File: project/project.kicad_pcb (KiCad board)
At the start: 4 copper layers, 64.5 x 86 mm, 186 parts, among them J101 BUS, J102 rs485, J103 qwiic, J104 FFC, J105 Bot, J106 FFC, J107 Top, J108 Mid, J109 Mid, J110 USB_C_Receptacle_USB2.0, J111 BUS, J201 5V, J202 24V, J203 3V3, J401 RJ45_Shielded, SW101 15mm, SW102 15mm, U101 TMP102, U102 24C02S, U103 USBLC6-2SC6, U104 TMP102, U105 INA226, U201 DP9700AT-24, U202 ME3121AM6G, U203 JTD6206-3.3V, U301 esp32-C3FH4X, U401 W5500, U501 XL1050, U601 MAX13487E, Y301 40MHz, Y401 25MHz

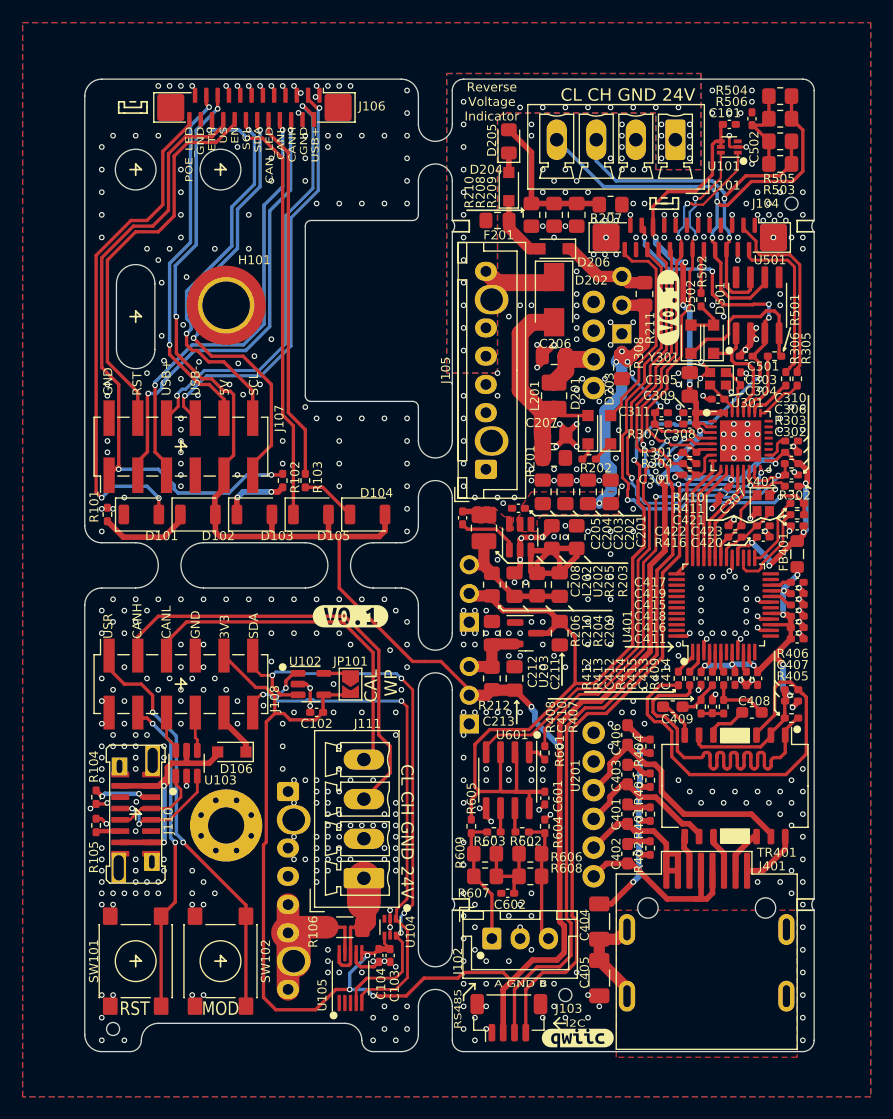
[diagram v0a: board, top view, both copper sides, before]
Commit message: fix PSU FB and tmp102 pinout
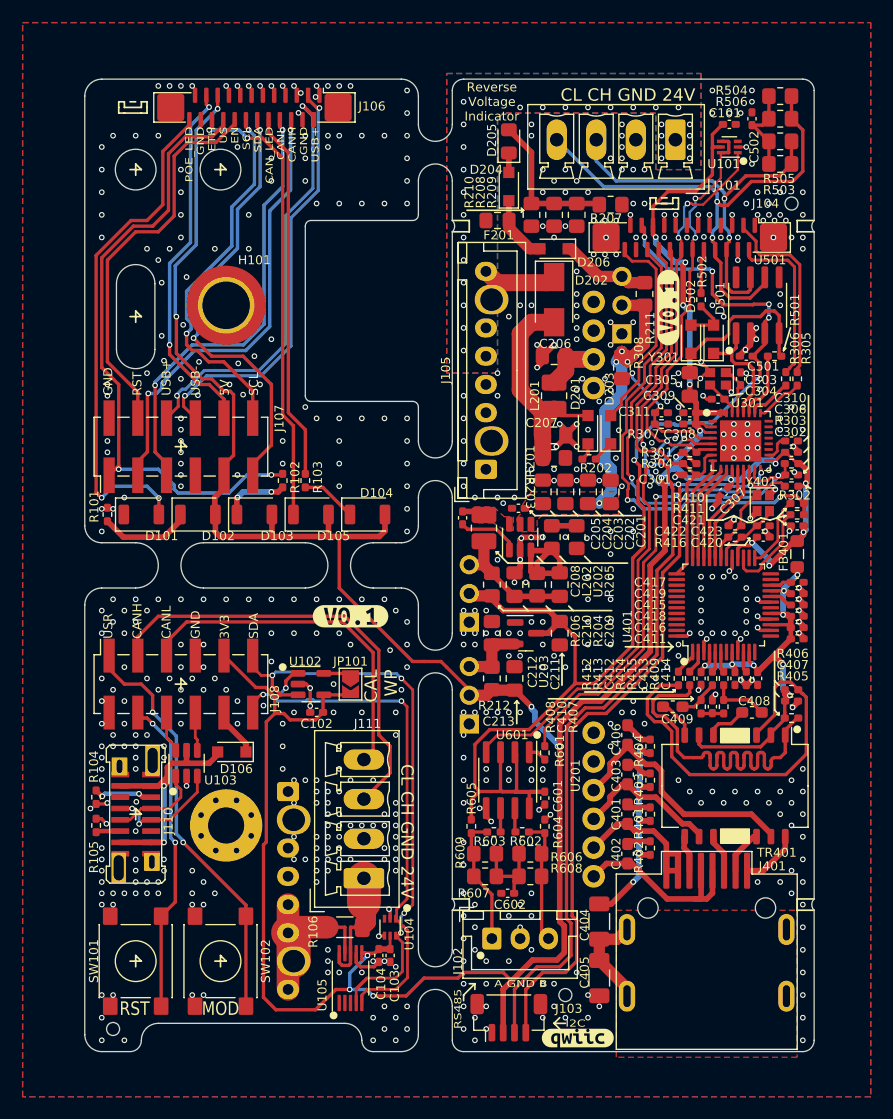
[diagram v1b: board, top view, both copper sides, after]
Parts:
- U101, U104: footprint Package_TO_SOT_SMD:SOT-563 -> -local:SOT-563
- turned R203 to -90 degrees
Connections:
- R203 pad 1: /PSU/FB -> Net-(R205-Pad2)
- R205 pad 2: GND -> Net-(R205-Pad2)
- U101 pad 4: 3V3 -> SDA
- U104 pad 4: 3V3 -> GND
- U104 pad 5: GND -> 3V3
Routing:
- net /PSU/FB: track 16.4 -> 11.4 mm
- net GND: track 63.2 -> 59.6 mm, vias 626 -> 623
- net SDA: track 96.2 -> 98.5 mm
- net Net-(R205-Pad2): track 0.00 -> 2.20 mm
